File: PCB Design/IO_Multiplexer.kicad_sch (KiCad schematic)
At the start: 45 parts, among them J42 Conn, J43 Conn_I2C, J45 Conn_01x04_Pin, J46 Conn_I2C, J47 Conn_Sig, U41 AMS1117-3.3, U42 SX1509BIULTRT, U43 TCA9406DC

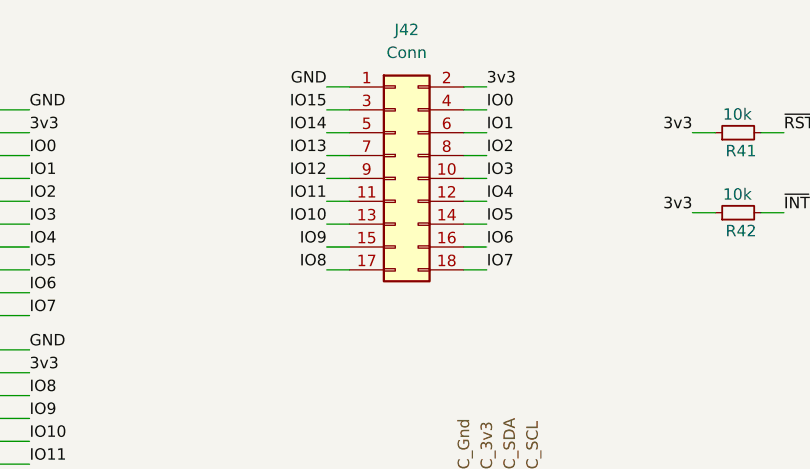
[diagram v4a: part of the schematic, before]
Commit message: Ready for production
Moved connectors to slightly overlap board edge
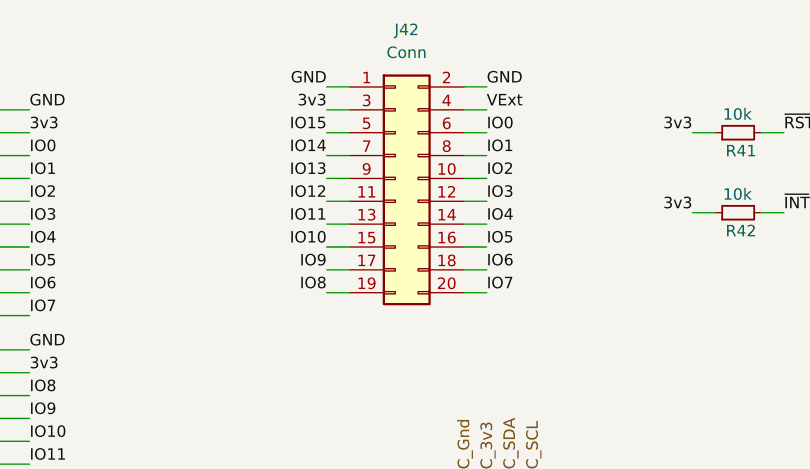
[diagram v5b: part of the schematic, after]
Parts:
- J42: footprint Connector_PinHeader_2.54mm:PinHeader_2x09_P2.54mm_Vertical -> Connector_IDC:IDC-Header_2x10_P2.54mm_Vertical; symbol Connector_Generic:Conn_02x09_Odd_Even -> Connector_Generic:Conn_02x10_Odd_Even
- J47: footprint Connector_JST:JST_XH_B4B-XH-A_1x04_P2.50mm_Vertical -> Connector_PinHeader_2.54mm:PinHeader_1x04_P2.54mm_Vertical
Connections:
- net 3v3: now also J42.3 (Pin_3); no longer J42.2 (Pin_2)
- net GND: now also J42.2 (Pin_2)
- net IO0: now also J42.6 (Pin_6); no longer J42.4 (Pin_4)
- net IO1: now also J42.8 (Pin_8); no longer J42.6 (Pin_6)
- net IO10: now also J42.15 (Pin_15); no longer J42.13 (Pin_13)
- net IO11: now also J42.13 (Pin_13); no longer J42.11 (Pin_11)
- net IO12: now also J42.11 (Pin_11); no longer J42.9 (Pin_9)
- net IO13: now also J42.9 (Pin_9); no longer J42.7 (Pin_7)
- net IO14: now also J42.7 (Pin_7); no longer J42.5 (Pin_5)
- net IO15: now also J42.5 (Pin_5); no longer J42.3 (Pin_3)
- net IO2: now also J42.10 (Pin_10); no longer J42.8 (Pin_8)
- net IO3: now also J42.12 (Pin_12); no longer J42.10 (Pin_10)
- net IO4: now also J42.14 (Pin_14); no longer J42.12 (Pin_12)
- net IO5: now also J42.16 (Pin_16); no longer J42.14 (Pin_14)
- net IO6: now also J42.18 (Pin_18); no longer J42.16 (Pin_16)
- net IO7: now also J42.20 (Pin_20); no longer J42.18 (Pin_18)
- net IO8: now also J42.19 (Pin_19); no longer J42.17 (Pin_17)
- net IO9: now also J42.17 (Pin_17); no longer J42.15 (Pin_15)
- net VExt: now also J42.4 (Pin_4)
